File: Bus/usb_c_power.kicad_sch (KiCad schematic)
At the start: 3 parts, among them J10 USB_C_Receptacle_PowerOnly_6P

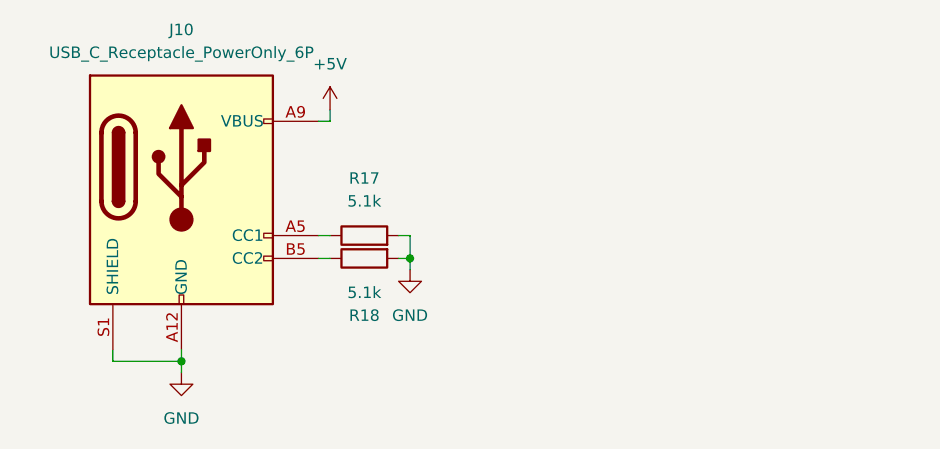
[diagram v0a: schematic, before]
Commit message: Updated bus schematics with pinout of MAR/ALU/Registers on PCBs ordered
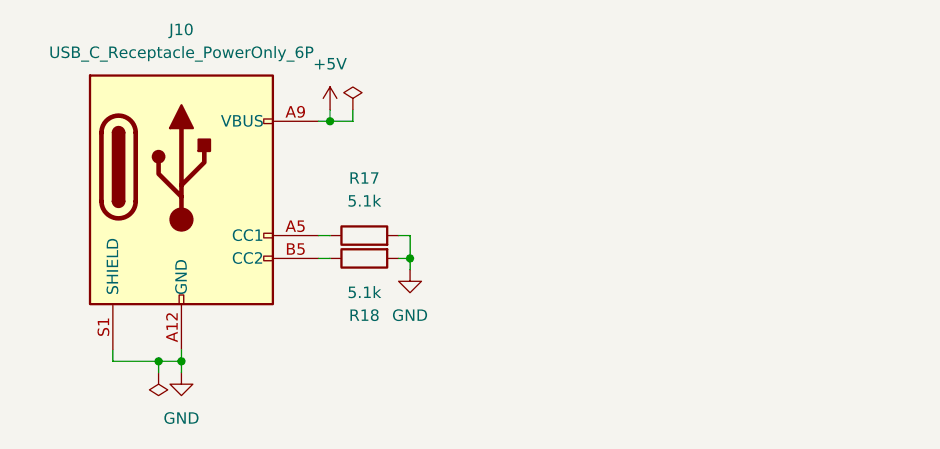
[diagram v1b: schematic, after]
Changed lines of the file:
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@@
 	(paper "A4")
+	(junction
+		(at 109.22 80.01)
+		(diameter 0)
+		(color 0 0 0 0)
+	)
 	(junction
 		(at 118.11 95.25)
@@
 	)
 	(junction
+		(at 90.17 106.68)
+		(diameter 0)
+		(color 0 0 0 0)
+	)
+	(junction
 		(at 92.71 106.68)
 		(diameter 0)
@@
 	(wire
 		(pts
+			(xy 111.76 80.01) (xy 109.22 80.01)
+		)
+		(stroke
+			(width 0)
+			(type default)
+		)
+	)
+	(wire
+		(pts
 			(xy 116.84 95.25) (xy 118.11 95.25)
 		)
@@
 	(wire
 		(pts
+			(xy 90.17 106.68) (xy 92.71 106.68)
+		)
+		(stroke
+			(width 0)
+			(type default)
+		)
+	)
+	(wire
+		(pts
 			(xy 118.11 92.71) (xy 116.84 92.71)
 		)
@@
 	(wire
 		(pts
+			(xy 111.76 78.74) (xy 111.76 80.01)
+		)
+		(stroke
+			(width 0)
+			(type default)
+		)
+	)
+	(wire
+		(pts
 			(xy 107.95 95.25) (xy 109.22 95.25)
 		)
@@
 	(wire
 		(pts
-			(xy 85.09 106.68) (xy 92.71 106.68)
+			(xy 90.17 106.68) (xy 90.17 107.95)
+		)
+		(stroke
+			(width 0)
+			(type default)
+		)
+	)
+	(wire
+		(pts
+			(xy 85.09 106.68) (xy 90.17 106.68)
 		)
 		(stroke
@@
 		(dnp no)
 		(fields_autoplaced yes)
-		(property "Reference" "#PWR010"
+		(property "Reference" "#PWR016"
 			(at 109.22 82.55 0)
 			(effects
@@
 			(project ""
 				(path "/37ae8b13-e183-404e-b70a-681e1af60f55/050af5a1-5dac-41e0-a6f2-7dd6742b296f"
-					(reference "#PWR010")
+					(reference "#PWR016")
+					(unit 1)
+				)
+			)
+		)
+	)
+	(symbol
+		(lib_id "power:PWR_FLAG")
+		(at 90.17 107.95 180)
+		(unit 1)
+		(exclude_from_sim no)
+		(in_bom yes)
+		(on_board yes)
+		(dnp no)
+		(fields_autoplaced yes)
+		(property "Reference" "#FLG02"
+			(at 90.17 109.855 0)
+			(effects
+				(font
+					(size 1.27 1.27)
+				)
+				(hide yes)
+			)
+		)
+		(property "Value" "PWR_FLAG"
+			(at 90.17 113.03 0)
+			(effects
+				(font
+					(size 1.27 1.27)
+				)
+				(hide yes)
+			)
+		)
+		(property "Footprint" ""
+			(at 90.17 107.95 0)
+			(effects
+				(font
+					(size 1.27 1.27)
+				)
+				(hide yes)
+			)
+		)
+		(property "Datasheet" "~"
+			(at 90.17 107.95 0)
+			(effects
+				(font
+					(size 1.27 1.27)
+				)
+				(hide yes)
+			)
+		)
+		(property "Description" "Special symbol for telling ERC where power comes from"
+			(at 90.17 107.95 0)
+			(effects
+				(font
+					(size 1.27 1.27)
+				)
+				(hide yes)
+			)
+		)
+		(pin "1"
+		)
+		(instances
+			(project "bus"
+				(path "/37ae8b13-e183-404e-b70a-681e1af60f55/050af5a1-5dac-41e0-a6f2-7dd6742b296f"
+					(reference "#FLG02")
 					(unit 1)
 				)
@@
 		(dnp no)
 		(fields_autoplaced yes)
-		(property "Reference" "#PWR011"
+		(property "Reference" "#PWR017"
 			(at 118.11 102.87 0)
 			(effects
@@
 			(project ""
 				(path "/37ae8b13-e183-404e-b70a-681e1af60f55/050af5a1-5dac-41e0-a6f2-7dd6742b296f"
-					(reference "#PWR011")
+					(reference "#PWR017")
+					(unit 1)
+				)
+			)
+		)
+	)
+	(symbol
+		(lib_id "power:PWR_FLAG")
+		(at 111.76 78.74 0)
+		(mirror y)
+		(unit 1)
+		(exclude_from_sim no)
+		(in_bom yes)
+		(on_board yes)
+		(dnp no)
+		(fields_autoplaced yes)
+		(property "Reference" "#FLG01"
+			(at 111.76 76.835 0)
+			(effects
+				(font
+					(size 1.27 1.27)
+				)
+				(hide yes)
+			)
+		)
+		(property "Value" "PWR_FLAG"
+			(at 111.76 73.66 0)
+			(effects
+				(font
+					(size 1.27 1.27)
+				)
+				(hide yes)
+			)
+		)
+		(property "Footprint" ""
+			(at 111.76 78.74 0)
+			(effects
+				(font
+					(size 1.27 1.27)
+				)
+				(hide yes)
+			)
+		)
+		(property "Datasheet" "~"
+			(at 111.76 78.74 0)
+			(effects
+				(font
+					(size 1.27 1.27)
+				)
+				(hide yes)
+			)
+		)
+		(property "Description" "Special symbol for telling ERC where power comes from"
+			(at 111.76 78.74 0)
+			(effects
+				(font
+					(size 1.27 1.27)
+				)
+				(hide yes)
+			)
+		)
+		(pin "1"
+		)
+		(instances
+			(project "bus"
+				(path "/37ae8b13-e183-404e-b70a-681e1af60f55/050af5a1-5dac-41e0-a6f2-7dd6742b296f"
+					(reference "#FLG01")
 					(unit 1)
 				)
@@
 		(dnp no)
 		(fields_autoplaced yes)
-		(property "Reference" "#PWR09"
+		(property "Reference" "#PWR015"
 			(at 92.71 114.3 0)
 			(effects
@@
 			(project "bus"
 				(path "/37ae8b13-e183-404e-b70a-681e1af60f55/050af5a1-5dac-41e0-a6f2-7dd6742b296f"
-					(reference "#PWR09")
-					(unit 1)
-				)
+					(reference "#PWR015")
+					(unit 1)
+				)

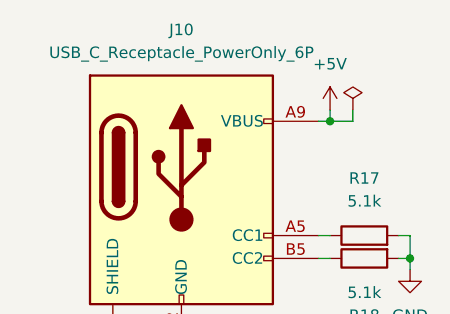
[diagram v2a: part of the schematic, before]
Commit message: Updated bus schmatic pins to match final layouts
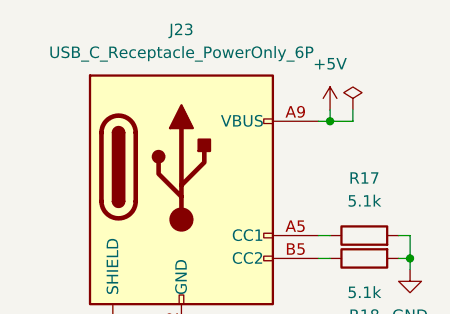
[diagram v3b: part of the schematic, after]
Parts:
- renumbered J10 to J23
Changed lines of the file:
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@@
 		(dnp no)
 		(fields_autoplaced yes)
-		(property "Reference" "J10"
+		(property "Reference" "J23"
 			(at 92.71 69.85 0)
 			(effects
@@
 			(project ""
 				(path "/37ae8b13-e183-404e-b70a-681e1af60f55/050af5a1-5dac-41e0-a6f2-7dd6742b296f"
-					(reference "J10")
+					(reference "J23")
 					(unit 1)
 				)
@@
 		(dnp no)
 		(fields_autoplaced yes)
-		(property "Reference" "#PWR014"
+		(property "Reference" "#PWR026"
 			(at 109.22 82.55 0)
 			(effects
@@
 			(project ""
 				(path "/37ae8b13-e183-404e-b70a-681e1af60f55/050af5a1-5dac-41e0-a6f2-7dd6742b296f"
-					(reference "#PWR014")
+					(reference "#PWR026")
 					(unit 1)
 				)
@@
 		(dnp no)
 		(fields_autoplaced yes)
-		(property "Reference" "#PWR015"
+		(property "Reference" "#PWR027"
 			(at 118.11 102.87 0)
 			(effects
@@
 			(project ""
 				(path "/37ae8b13-e183-404e-b70a-681e1af60f55/050af5a1-5dac-41e0-a6f2-7dd6742b296f"
-					(reference "#PWR015")
+					(reference "#PWR027")
 					(unit 1)
 				)
@@
 		(dnp no)
 		(fields_autoplaced yes)
-		(property "Reference" "#PWR013"
+		(property "Reference" "#PWR025"
 			(at 92.71 114.3 0)
 			(effects
@@
 			(project "bus"
 				(path "/37ae8b13-e183-404e-b70a-681e1af60f55/050af5a1-5dac-41e0-a6f2-7dd6742b296f"
-					(reference "#PWR013")
-					(unit 1)
-				)
+					(reference "#PWR025")
+					(unit 1)
+				)

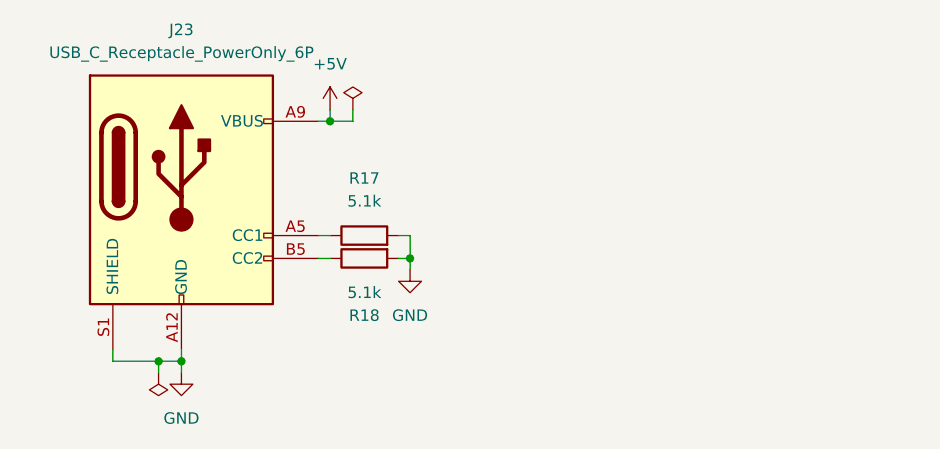
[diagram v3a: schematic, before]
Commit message: Added an extra power option if I can't solder the USB header
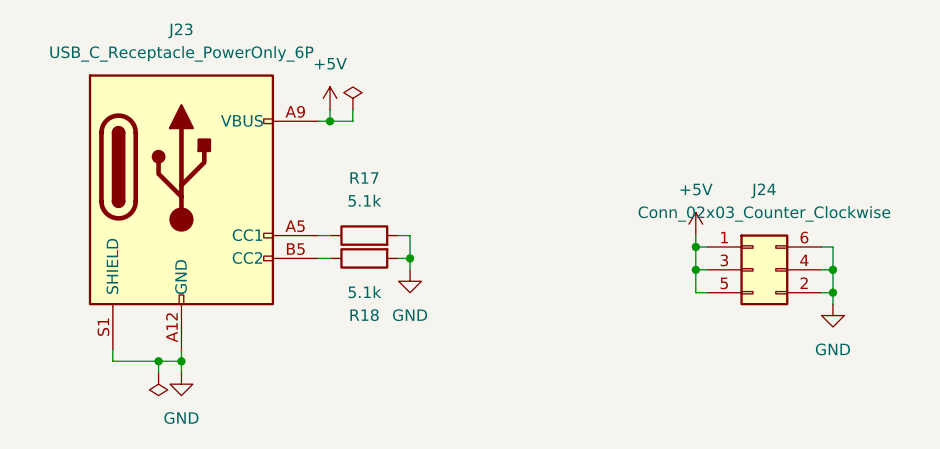
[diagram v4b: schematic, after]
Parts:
- added J24: Conn_02x03_Counter_Clockwise, Connector_PinHeader_2.54mm:PinHeader_2x03_P2.54mm_Vertical, symbol Connector_Generic:Conn_02x03_Counter_Clockwise
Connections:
- net +5V: now also J24.1 (Pin_1), J24.3 (Pin_2), J24.5 (Pin_3)
- net GND: now also J24.2 (Pin_4), J24.4 (Pin_5), J24.6 (Pin_6)
